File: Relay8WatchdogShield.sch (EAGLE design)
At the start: 9 parts, among them J1 Digital_0_7, J2 Analog, J3 Digital_8_13, J4 Analog

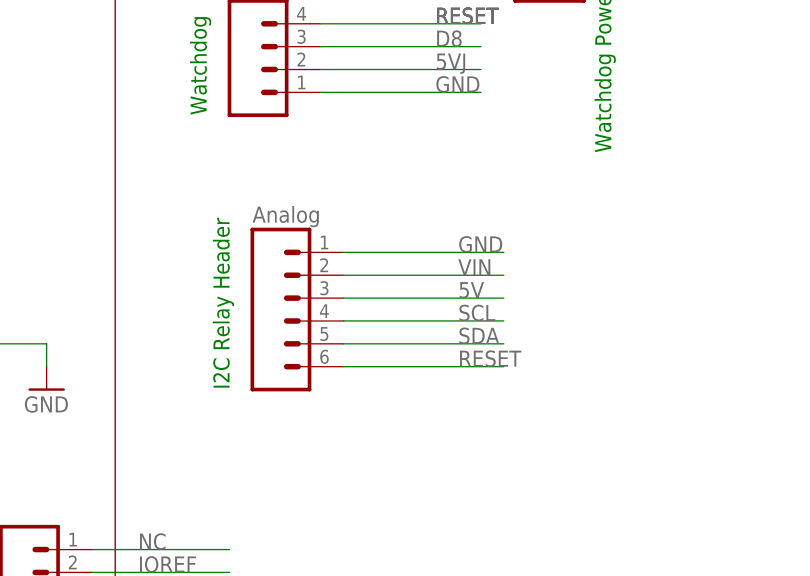
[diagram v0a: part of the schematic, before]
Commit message: Updated I2c Header
Changed Header from 1x6 to 2x3 IDC Shrouded Header.
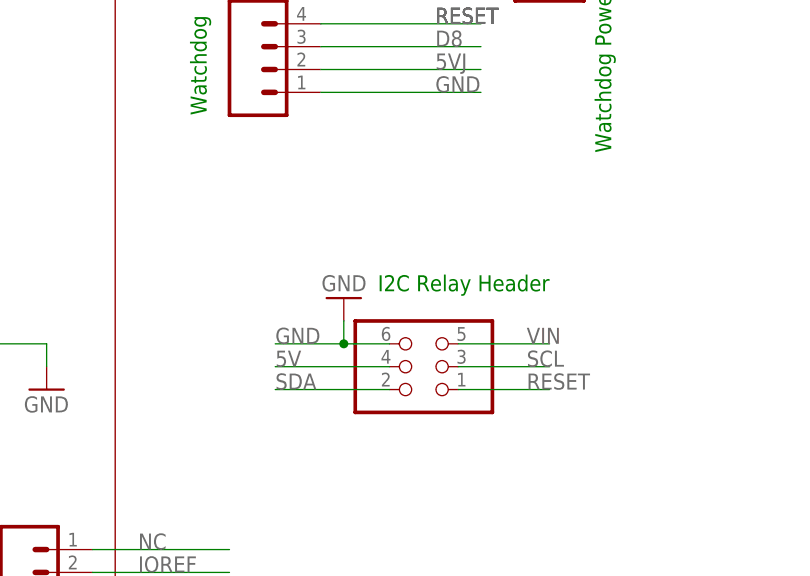
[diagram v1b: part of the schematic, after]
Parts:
- removed J4: Analog, freetronics:M06SIP
- added JP4: (no value), pinhead:PINHD-2X3
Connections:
- net 5V: now also JP4.4; no longer J4.3
- net GND: now also JP4.6; no longer J4.1
- net RESET: now also JP4.1; no longer J4.6
- net SCL: now also JP4.3; no longer J4.4
- net SDA: now also JP4.2; no longer J4.5
- net VIN: now also JP4.5; no longer J4.2
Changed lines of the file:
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@@
 <?xml version="1.0" encoding="utf-8"?>
 <!DOCTYPE eagle SYSTEM "eagle.dtd">
-<eagle version="9.4.2">
+<eagle version="9.5.0">
 <drawing>
 <settings>
@@
 <layer number="112" name="tSilk" color="7" fill="1" visible="no" active="yes"/>
 <layer number="113" name="ReferenceLS" color="7" fill="1" visible="no" active="no"/>
+<layer number="114" name="Badge_Outline" color="7" fill="1" visible="no" active="yes"/>
+<layer number="115" name="ReferenceISLANDS" color="7" fill="1" visible="no" active="yes"/>
 <layer number="116" name="Patch_BOT" color="9" fill="4" visible="yes" active="yes"/>
+<layer number="117" name="BACKMAAT1" color="7" fill="1" visible="no" active="no"/>
 <layer number="118" name="Rect_Pads" color="7" fill="1" visible="no" active="no"/>
+<layer number="119" name="KAP_TEKEN" color="7" fill="1" visible="no" active="no"/>
+<layer number="120" name="KAP_MAAT1" color="7" fill="1" visible="no" active="no"/>
 <layer number="121" name="_tsilk" color="7" fill="1" visible="yes" active="yes"/>
 <layer number="122" name="_bsilk" color="7" fill="1" visible="yes" active="yes"/>
@@
 <layer number="128" name="_bValues" color="7" fill="1" visible="no" active="yes"/>
 <layer number="129" name="Mask" color="7" fill="1" visible="yes" active="yes"/>
+<layer number="130" name="SMDSTROOK" color="7" fill="1" visible="no" active="no"/>
 <layer number="131" name="tAdjust" color="7" fill="1" visible="no" active="yes"/>
 <layer number="132" name="bAdjust" color="7" fill="1" visible="no" active="yes"/>
+<layer number="133" name="bottom_silk" color="7" fill="1" visible="no" active="no"/>
+<layer number="134" name="silk_top" color="5" fill="1" visible="yes" active="yes"/>
+<layer number="135" name="silk_bottom" color="7" fill="1" visible="no" active="no"/>
+<layer number="136" name="silktop" color="7" fill="1" visible="yes" active="yes"/>
+<layer number="137" name="silkbottom" color="7" fill="1" visible="yes" active="yes"/>
+<layer number="138" name="mbTest" color="7" fill="1" visible="yes" active="yes"/>
+<layer number="139" name="mtKeepout" color="7" fill="1" visible="yes" active="yes"/>
+<layer number="140" name="mbKeepout" color="7" fill="1" visible="yes" active="yes"/>
+<layer number="141" name="mtRestrict" color="7" fill="1" visible="yes" active="yes"/>
+<layer number="142" name="mbRestrict" color="7" fill="1" visible="yes" active="yes"/>
+<layer number="143" name="mvRestrict" color="7" fill="1" visible="yes" active="yes"/>
 <layer number="144" name="Drill_legend" color="7" fill="1" visible="no" active="yes"/>
+<layer number="145" name="DrillLegend_01-16" color="7" fill="1" visible="yes" active="yes"/>
+<layer number="146" name="DrillLegend_01-20" color="7" fill="1" visible="yes" active="yes"/>
+<layer number="147" name="mMeasures" color="7" fill="1" visible="yes" active="yes"/>
+<layer number="148" name="mDocument" color="7" fill="1" visible="yes" active="yes"/>
+<layer number="149" name="mReference" color="7" fill="1" visible="yes" active="yes"/>
 <layer number="150" name="Notes" color="7" fill="1" visible="no" active="yes"/>
 <layer number="151" name="HeatSink" color="7" fill="1" visible="yes" active="yes"/>
@@
 <layer number="154" name="FabDoc2" color="2" fill="1" visible="no" active="no"/>
 <layer number="155" name="FabDoc3" color="7" fill="15" visible="no" active="no"/>
+<layer number="166" name="AntennaArea" color="7" fill="1" visible="yes" active="yes"/>
+<layer number="168" name="4mmHeightArea" color="7" fill="1" visible="yes" active="yes"/>
+<layer number="191" name="mNets" color="7" fill="1" visible="yes" active="yes"/>
+<layer number="192" name="mBusses" color="7" fill="1" visible="yes" active="yes"/>
+<layer number="193" name="mPins" color="7" fill="1" visible="yes" active="yes"/>
+<layer number="194" name="mSymbols" color="7" fill="1" visible="yes" active="yes"/>
+<layer number="195" name="mNames" color="7" fill="1" visible="yes" active="yes"/>
+<layer number="196" name="mValues" color="7" fill="1" visible="yes" active="yes"/>
 <layer number="199" name="Contour" color="7" fill="1" visible="no" active="yes"/>
 <layer number="200" name="200bmp" color="1" fill="10" visible="no" active="no"/>
@@
 <part name="JP1" library="adafruit" library_urn="urn:adsk.eagle:library:420" deviceset="PINHD-1X1" device="" package3d_urn="urn:adsk.eagle:package:6240654/1"/>
 <part name="JP2" library="adafruit" library_urn="urn:adsk.eagle:library:420" deviceset="PINHD-1X1" device="" package3d_urn="urn:adsk.eagle:package:6240654/1"/>
-<part name="J4" library="freetronics" deviceset="M06" device="SIP" value="Analog"/>
 <part name="JP3" library="EtherMegaR3" deviceset="FREETRONICS-MASTER-V1_M04" device="PTH"/>
+<part name="JP4" library="pinhead" library_urn="urn:adsk.eagle:library:325" deviceset="PINHD-2X3" device="" package3d_urn="urn:adsk.eagle:package:22462/2"/>
+<part name="GND2" library="freetronics" deviceset="GND" device=""/>
 </parts>
 <sheets>
@@
 <frame x1="213.36" y1="5.08" x2="243.84" y2="10.16" columns="8" rows="5" layer="94"/>
 <text x="60.96" y="139.7" size="1.778" layer="91" rot="R90">Watchdog</text>
-<text x="63.5" y="109.22" size="1.778" layer="91" rot="R90">I2C Relay Header</text>
+<text x="99.06" y="121.92" size="1.778" layer="91" rot="R180">I2C Relay Header</text>
 <text x="104.14" y="162.56" size="1.778" layer="91" rot="R270">Watchdog Power Jumper</text>
 </plain>
@@
 <attribute name="VALUE" x="95.25" y="149.86" size="1.778" layer="96"/>
 </instance>
-<instance part="J4" gate="G$1" x="71.12" y="119.38" smashed="yes" rot="MR180">
-<attribute name="VALUE" x="66.04" y="129.54" size="1.778" layer="96" rot="MR180"/>
-</instance>
 <instance part="JP3" gate="G$1" x="68.58" y="144.78" smashed="yes">
 <attribute name="VALUE" x="63.5" y="137.16" size="1.778" layer="96"/>
+</instance>
+<instance part="JP4" gate="A" x="86.36" y="111.76" smashed="yes" rot="R180">
+<attribute name="VALUE" x="92.71" y="119.38" size="1.778" layer="96" rot="R180"/>
+</instance>
+<instance part="GND2" gate="1" x="76.2" y="119.38" smashed="yes" rot="R180">
+<attribute name="VALUE" x="78.74" y="121.92" size="1.778" layer="96" rot="R180"/>
 </instance>
 </instances>
@@
 </segment>
 <segment>
-<wire x1="76.2" y1="119.38" x2="93.98" y2="119.38" width="0.1524" layer="91"/>
-<label x="88.9" y="119.38" size="1.778" layer="95"/>
-<pinref part="J4" gate="G$1" pin="3"/>
+<pinref part="JP4" gate="A" pin="4"/>
+<wire x1="81.28" y1="111.76" x2="68.58" y2="111.76" width="0.1524" layer="91"/>
+<label x="68.58" y="111.76" size="1.778" layer="95"/>
 </segment>
 </net>
@@
 </segment>
 <segment>
-<wire x1="76.2" y1="124.46" x2="93.98" y2="124.46" width="0.1524" layer="91"/>
-<label x="88.9" y="124.46" size="1.778" layer="95"/>
-<pinref part="J4" gate="G$1" pin="1"/>
+<pinref part="JP4" gate="A" pin="6"/>
+<wire x1="81.28" y1="114.3" x2="76.2" y2="114.3" width="0.1524" layer="91"/>
+<label x="68.58" y="114.3" size="1.778" layer="95"/>
+<pinref part="GND2" gate="1" pin="GND"/>
+<wire x1="76.2" y1="114.3" x2="68.58" y2="114.3" width="0.1524" layer="91"/>
+<wire x1="76.2" y1="116.84" x2="76.2" y2="114.3" width="0.1524" layer="91"/>
+<junction x="76.2" y="114.3"/>
 </segment>
 </net>
@@
 </segment>
 <segment>
-<wire x1="76.2" y1="121.92" x2="93.98" y2="121.92" width="0.1524" layer="91"/>
-<label x="88.9" y="121.92" size="1.778" layer="95"/>
-<pinref part="J4" gate="G$1" pin="2"/>
+<pinref part="JP4" gate="A" pin="5"/>
+<wire x1="88.9" y1="114.3" x2="99.06" y2="114.3" width="0.1524" layer="91"/>
+<label x="96.52" y="114.3" size="1.778" layer="95"/>
 </segment>
 </net>
@@
 </segment>
 <segment>
-<wire x1="76.2" y1="111.76" x2="93.98" y2="111.76" width="0.1524" layer="91"/>
-<label x="88.9" y="111.76" size="1.778" layer="95"/>
-<pinref part="J4" gate="G$1" pin="6"/>
+<pinref part="JP4" gate="A" pin="1"/>
+<wire x1="88.9" y1="109.22" x2="99.06" y2="109.22" width="0.1524" layer="91"/>
+<label x="96.52" y="109.22" size="1.778" layer="95"/>
 </segment>
 </net>
@@
 </segment>
 <segment>
-<wire x1="76.2" y1="114.3" x2="93.98" y2="114.3" width="0.1524" layer="91"/>
-<label x="88.9" y="114.3" size="1.778" layer="95"/>
-<pinref part="J4" gate="G$1" pin="5"/>
+<pinref part="JP4" gate="A" pin="2"/>
+<wire x1="81.28" y1="109.22" x2="68.58" y2="109.22" width="0.1524" layer="91"/>
+<label x="68.58" y="109.22" size="1.778" layer="95"/>
 </segment>
 </net>
@@
 </segment>
 <segment>
-<wire x1="76.2" y1="116.84" x2="93.98" y2="116.84" width="0.1524" layer="91"/>
-<label x="88.9" y="116.84" size="1.778" layer="95"/>
-<pinref part="J4" gate="G$1" pin="4"/>
-</segment>
-</net>
+<pinref part="JP4" gate="A" pin="3"/>
+<wire x1="88.9" y1="111.76" x2="99.06" y2="111.76" width="0.1524" layer="91"/>
+<label x="96.52" y="111.76" size="1.778" layer="95"/>
+</segment>
+</net>
